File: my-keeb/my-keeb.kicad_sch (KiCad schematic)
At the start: 166 parts, among them SW1 SW_Push, SW10 SW_Push, SW11 SW_Push, SW12 SW_Push, SW13 SW_Push, SW14 SW_Push, SW15 SW_Push, SW16 SW_Push, SW17 SW_Push, SW18 SW_Push, SW19 SW_Push, SW2 SW_Push, SW20 SW_Push, SW21 SW_Push, SW22 SW_Push, SW23 SW_Push, SW24 SW_Push, SW25 SW_Push, SW26 SW_Push, SW27 SW_Push, SW28 SW_Push, SW29 SW_Push, SW3 SW_Push, SW30 SW_Push, SW31 SW_Push, SW32 SW_Push, SW33 SW_Push, SW34 SW_Push, SW35 SW_Push, SW36 SW_Push, SW37 SW_Push, SW38 SW_Push, SW39 SW_Push, SW4 SW_Push, SW40 SW_Push, SW41 SW_Push, SW42 SW_Push, SW43 SW_Push, SW44 SW_Push, SW45 SW_Push, SW46 SW_Push, SW47 SW_Push, SW48 SW_Push, SW49 SW_Push, SW5 SW_Push, SW50 SW_Push, SW51 SW_Push, SW52 SW_Push, SW53 SW_Push, SW54 SW_Push, SW55 SW_Push, SW56 SW_Push, SW57 SW_Push, SW58 SW_Push, SW59 SW_Push, SW6 SW_Push, SW60 SW_Push, SW61 SW_Push, SW62 SW_Push, SW63 SW_Push, SW64 SW_Push, SW65 SW_Push, SW66 SW_Push, SW67 SW_Push, SW68 SW_Push, SW69 SW_Push, SW7 SW_Push, SW70 SW_Push, SW71 SW_Push, SW72 SW_Push, SW73 SW_Push, SW74 SW_Push, SW75 SW_Push, SW76 SW_Push, SW77 SW_Push, SW78 SW_Push, SW79 SW_Push, SW8 SW_Push, SW80 RotaryEncoder, SW81 SW_Push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

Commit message: Finishing schematic
Changed rotary encoder to reflect EC11, altered some things, updated JOURNAL.md. Nothing makes sence i don't understand where to wire the screen and knob?
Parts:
- removed SW80: RotaryEncoder, symbol Device:RotaryEncoder
- added SW80: RotaryEncoder_Switch, symbol Device:RotaryEncoder_Switch
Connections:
- net COL10: now also A1.21 (GPIO16)
- net COL11: now also A1.22 (GPIO17); no longer A1.21 (GPIO16)
- net COL12: now also A1.24 (GPIO18); no longer A1.22 (GPIO17)
- net COL13: now also A1.25 (GPIO19); no longer A1.24 (GPIO18)
- net COL14: now also A1.26 (GPIO20); no longer A1.25 (GPIO19)
- net GND: now reaches A1.13 (GND), A1.18 (GND), A1.23 (GND), A1.28 (GND), A1.3 (GND), A1.38 (GND), A1.8 (GND)
- net GND: now also SW80.C, SW80.S2
- net ENC_A: now reaches A1.27 (GPIO21)
- net ENC_A: now also SW80.A
- net ENC_B: now reaches A1.29 (GPIO22)
- net ENC_B: now also SW80.B
- net ENC_SW: now reaches A1.34 (GPIO28_ADC2)
- net ENC_SW: now also SW80.S1
- net +3V3: now reaches A1.36 (3V3)

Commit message: Made the schematic more spacious and larger, removed page up and down keys because I've never used them before, finally onto the stabilizer step in the documentation at 2:38
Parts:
- removed D80, D81: 1N4148, Diode_THT:D_DO-35_SOD27_P7.62mm_Horizontal, symbol Diode:1N4148
- removed SW81, SW82: SW_Push, symbol Switch:SW_Push
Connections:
- net +3V3: now also U1.2 (VCC)
- net COL0: now also A1.9 (GPIO6), SW1.1, SW15.1, SW29.1, SW43.1, SW57.1, SW71.1
- net COL1: now also A1.10 (GPIO7), SW16.1, SW2.1, SW30.1, SW44.1, SW58.1, SW72.1
- net COL10: now also SW11.1, SW25.1, SW39.1, SW53.1, SW67.1, SW75.1
- net COL11: now also SW12.1, SW26.1, SW40.1, SW54.1, SW68.1
- net COL12: now also SW13.1, SW27.1, SW41.1, SW55.1, SW69.1, SW76.1
- net COL13: now also SW14.1, SW28.1, SW42.1, SW56.1, SW70.1, SW77.1
- net COL14: now also SW78.1
- net COL2: now also A1.11 (GPIO8), SW17.1, SW3.1, SW31.1, SW45.1, SW59.1, SW73.1
- net COL3: now also A1.12 (GPIO9), SW18.1, SW32.1, SW4.1, SW46.1, SW60.1
- net COL4: now also A1.14 (GPIO10), SW19.1, SW33.1, SW47.1, SW5.1, SW61.1
- net COL5: now also A1.15 (GPIO11), SW20.1, SW34.1, SW48.1, SW6.1, SW62.1
- net COL6: now also A1.16 (GPIO12), SW21.1, SW35.1, SW49.1, SW63.1, SW7.1, SW79.1
- net COL7: now also A1.17 (GPIO13), SW22.1, SW36.1, SW50.1, SW64.1, SW8.1
- net COL8: now also A1.19 (GPIO14), SW23.1, SW37.1, SW51.1, SW65.1, SW9.1
- net COL9: now also A1.20 (GPIO15), SW10.1, SW24.1, SW38.1, SW52.1, SW66.1, SW74.1
- net GND: now also U1.1 (GND)
- net ROW0: now also A1.1 (GPIO0)
- net ROW1: now also A1.2 (GPIO1), D15.1 (K), D16.1 (K), D17.1 (K), D18.1 (K), D19.1 (K), D20.1 (K), D21.1 (K), D22.1 (K), D23.1 (K), D24.1 (K), D25.1 (K), D26.1 (K), D27.1 (K), D28.1 (K)
- net ROW2: now also A1.4 (GPIO2), D29.1 (K), D30.1 (K), D31.1 (K), D32.1 (K), D33.1 (K), D34.1 (K), D35.1 (K), D36.1 (K), D37.1 (K), D38.1 (K), D39.1 (K), D40.1 (K), D41.1 (K), D42.1 (K)
- net ROW3: now also A1.5 (GPIO3), D43.1 (K), D44.1 (K), D45.1 (K), D46.1 (K), D47.1 (K), D48.1 (K), D49.1 (K), D50.1 (K), D51.1 (K), D52.1 (K), D53.1 (K), D54.1 (K), D55.1 (K), D56.1 (K)
- net ROW4: now also A1.6 (GPIO4), D57.1 (K), D58.1 (K), D59.1 (K), D60.1 (K), D61.1 (K), D62.1 (K), D63.1 (K), D64.1 (K), D65.1 (K), D66.1 (K), D67.1 (K), D68.1 (K), D69.1 (K), D70.1 (K)
- net ROW5: now also A1.7 (GPIO5), D71.1 (K), D72.1 (K), D73.1 (K), D74.1 (K), D75.1 (K), D76.1 (K), D77.1 (K), D78.1 (K), D79.1 (K)
- net SDA: now reaches A1.31 (GPIO26_ADC0)
- net SDA: now also U1.4 (SDA)
- net SCL: now reaches A1.32 (GPIO27_ADC1)
- net SCL: now also U1.3 (SCL)
- no-connect marks 0 -> 6
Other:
- moved on the sheet: A1, D1, D10, D11, D12, D13, D14, D15, D16, D17, D18, D19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

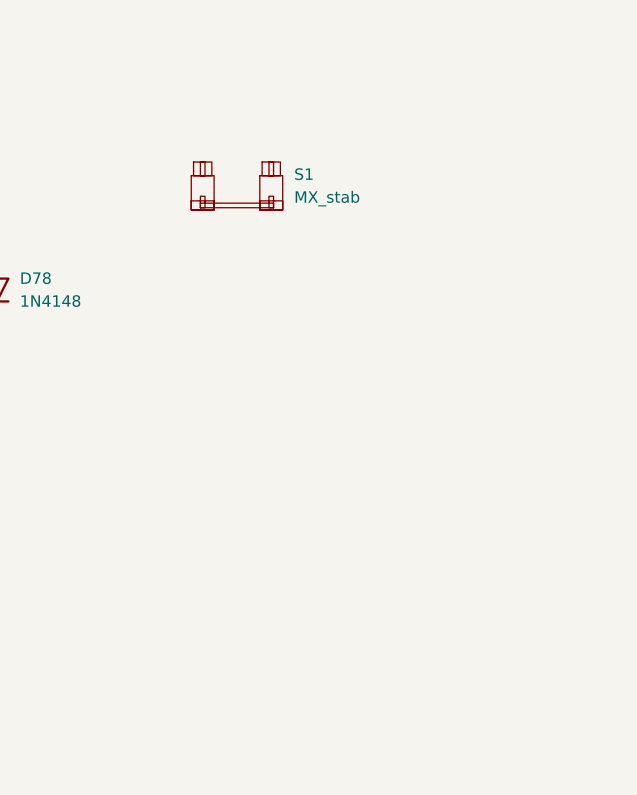
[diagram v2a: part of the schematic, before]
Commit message: Updated Journal and schematics
Created mounting holes and stabilizers
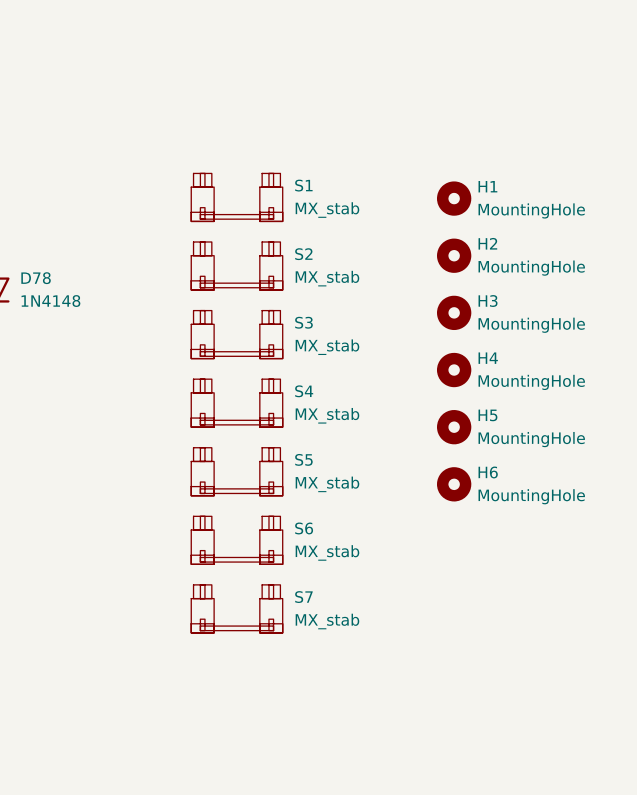
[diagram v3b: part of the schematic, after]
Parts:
- added H1, H2, H3, H4, H5, H6: MountingHole, symbol Mechanical:MountingHole
- added S2, S3, S4, S5, S6, S7: MX_stab, PCM_marbastlib-mx:STAB_MX_P_6.25u, symbol PCM_marbastlib-mx:MX_stab
- A1: footprint Module:RaspberryPi_Pico_Common_Unspecified -> Module:RaspberryPi_Pico_Common_THT
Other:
- moved on the sheet: S1

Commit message: assigned foot prints
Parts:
- removed H6: MountingHole, symbol Mechanical:MountingHole
- removed S5, S6, S7: MX_stab, PCM_marbastlib-mx:STAB_MX_P_6.25u, symbol PCM_marbastlib-mx:MX_stab
- S1, S2, S3: footprint PCM_marbastlib-mx:STAB_MX_P_6.25u -> PCM_marbastlib-mx:STAB_MX_2u
- S4: footprint PCM_marbastlib-mx:STAB_MX_P_6.25u -> PCM_marbastlib-mx:STAB_MX_6.25u
- SW1, SW10, SW11, SW12, SW13, SW14, SW15, SW16, SW17, SW18, SW19, SW2, SW20, SW21, SW22, SW23, SW24, SW25, SW26, SW27, SW28, SW29, SW3, SW30, SW31, SW32, SW33, SW34, SW35, SW36, SW37, SW38, SW39, SW4, SW40, SW41, SW42, SW43, SW44, SW45, SW46, SW47, SW48, SW49, SW5, SW50, SW51, SW52, SW53, SW54, SW55, SW56, SW57, SW58, SW59, SW6, SW60, SW61, SW62, SW63, SW64, SW65, SW66, SW67, SW68, SW69, SW7, SW70, SW71, SW72, SW73, SW74, SW75, SW76, SW77, SW78, SW79, SW8, SW9: footprint (none) -> PCM_marbastlib-mx:SW_MX_1u
